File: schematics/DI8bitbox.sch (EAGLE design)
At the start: 20 parts, among them Q1 500mA/300V, X1 332-02, X2 332-02

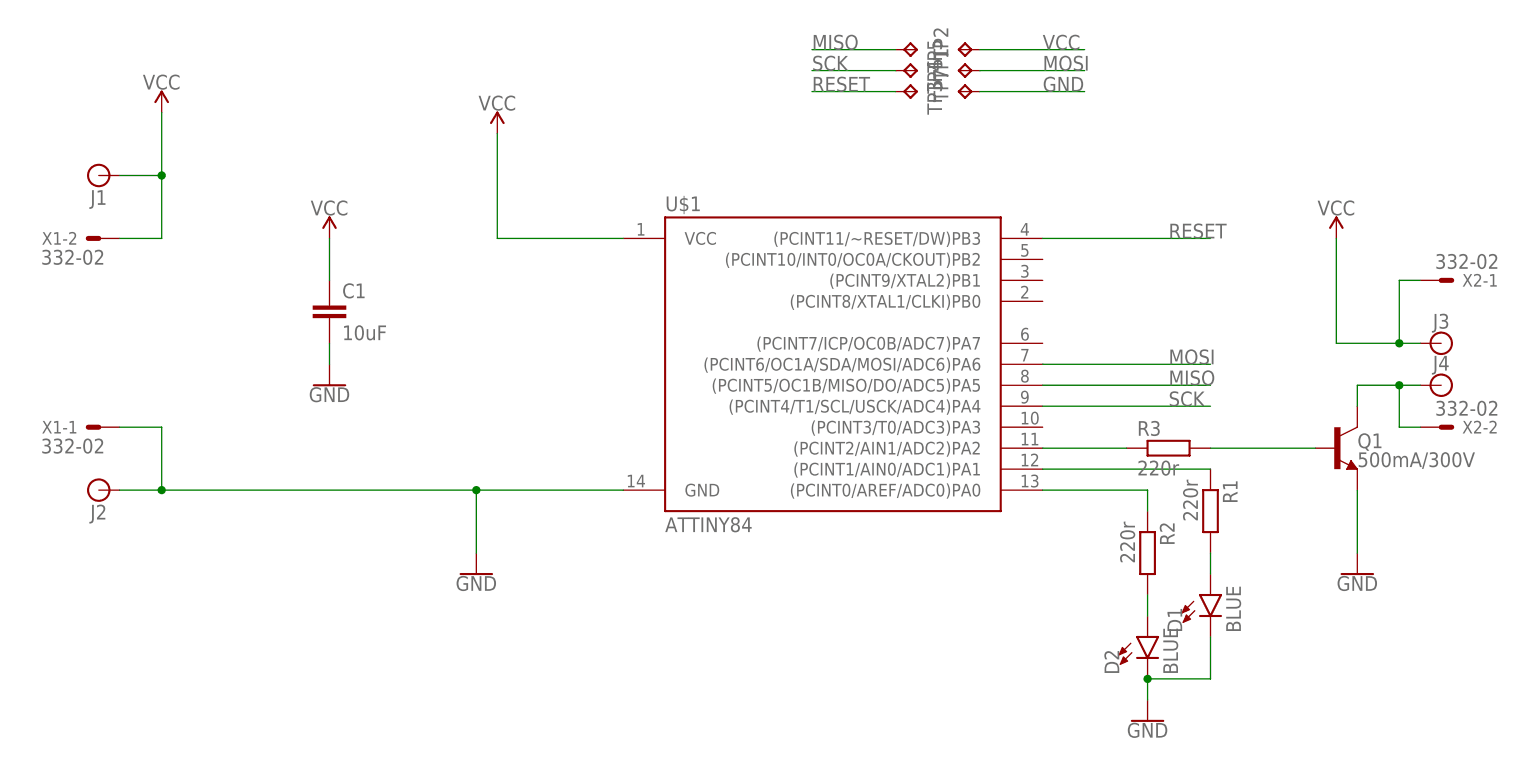
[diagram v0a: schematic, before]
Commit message: ordered rev.b at safepcb and mouser BOM updated
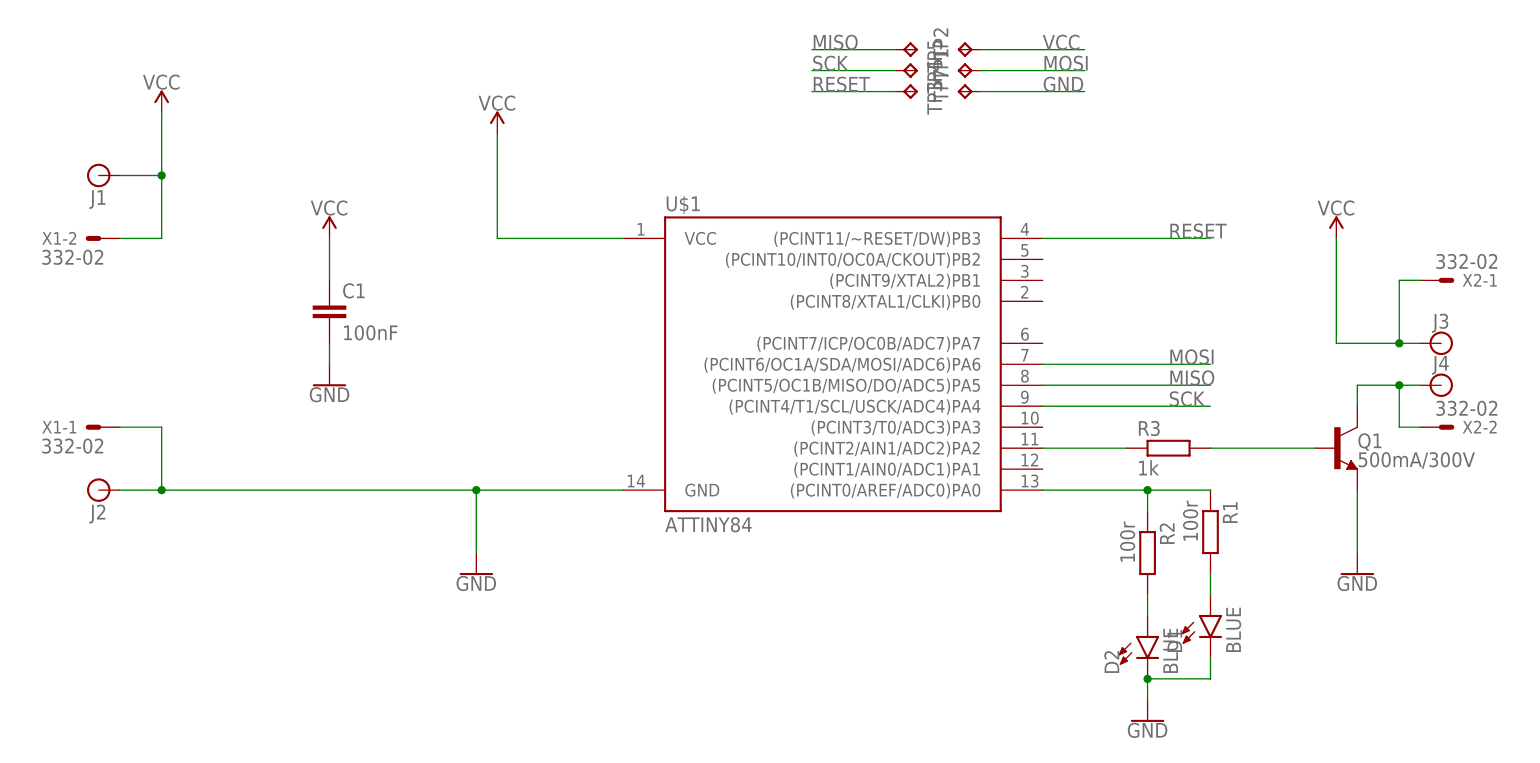
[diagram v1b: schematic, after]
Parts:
- C1: value 10uF -> 100nF; device SparkFun-Capacitors:10UF-1210-50V-20% -> SparkFun-Capacitors:10UF-1206-6.3V-20%
- R1, R2: value 220r -> 100r
- R3: value 220r -> 1k
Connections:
- removed net N$4: R1.1, U$1.(PCINT1/AIN0/ADC1)PA1
- net N$1: now also R1.1
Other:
- moved on the sheet: D1, R1
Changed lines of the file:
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@@
 <part name="GND1" library="SparkFun-PowerSymbols" deviceset="GND" device=""/>
 <part name="SUPPLY1" library="SparkFun-PowerSymbols" deviceset="VCC" device=""/>
-<part name="R1" library="rcl" deviceset="R-EU_" device="M0805" value="220r"/>
-<part name="R2" library="rcl" deviceset="R-EU_" device="M0805" value="220r"/>
+<part name="R1" library="rcl" deviceset="R-EU_" device="M0805" value="100r"/>
+<part name="R2" library="rcl" deviceset="R-EU_" device="M0805" value="100r"/>
 <part name="D1" library="SparkFun-LED" deviceset="LED-BLUE" device="1206" value="BLUE"/>
 <part name="D2" library="SparkFun-LED" deviceset="LED-BLUE" device="1206" value="BLUE"/>
@@
 <part name="SUPPLY4" library="SparkFun-PowerSymbols" deviceset="VCC" device=""/>
 <part name="GND5" library="SparkFun-PowerSymbols" deviceset="GND" device=""/>
-<part name="C1" library="SparkFun-Capacitors" deviceset="10UF" device="-1210-50V-20%" value="10uF"/>
+<part name="C1" library="SparkFun-Capacitors" deviceset="10UF" device="-1206-6.3V-20%" value="100nF"/>
 <part name="TP7" library="testpad" deviceset="TP" device="TP18R"/>
 <part name="TP1" library="testpad" deviceset="TP" device="TP18R"/>
@@
 <part name="J4" library="SparkFun-Connectors" deviceset="BANANA_CONN" device=""/>
 <part name="X2" library="con-garry" deviceset="332-02" device=""/>
-<part name="R3" library="rcl" deviceset="R-EU_" device="M0805" value="220r"/>
+<part name="R3" library="rcl" deviceset="R-EU_" device="M0805" value="1k"/>
 </parts>
 <sheets>
@@
 <instance part="GND1" gate="1" x="12.7" y="25.4"/>
 <instance part="SUPPLY1" gate="G$1" x="15.24" y="78.74"/>
-<instance part="R1" gate="G$1" x="101.6" y="33.02" rot="R270"/>
+<instance part="R1" gate="G$1" x="101.6" y="30.48" rot="R270"/>
 <instance part="R2" gate="G$1" x="93.98" y="27.94" rot="R270"/>
-<instance part="D1" gate="G$1" x="101.6" y="22.86"/>
+<instance part="D1" gate="G$1" x="101.6" y="20.32"/>
 <instance part="D2" gate="G$1" x="93.98" y="17.78"/>
 <instance part="GND3" gate="1" x="93.98" y="7.62"/>
@@
 <wire x1="93.98" y1="12.7" x2="93.98" y2="10.16" width="0.1524" layer="91"/>
 <pinref part="D1" gate="G$1" pin="C"/>
-<wire x1="101.6" y1="17.78" x2="101.6" y2="12.7" width="0.1524" layer="91"/>
+<wire x1="101.6" y1="15.24" x2="101.6" y2="12.7" width="0.1524" layer="91"/>
 <wire x1="101.6" y1="12.7" x2="93.98" y2="12.7" width="0.1524" layer="91"/>
 <junction x="93.98" y="12.7"/>
@@
 <pinref part="R2" gate="G$1" pin="1"/>
 <wire x1="93.98" y1="35.56" x2="93.98" y2="33.02" width="0.1524" layer="91"/>
+<pinref part="R1" gate="G$1" pin="1"/>
+<wire x1="93.98" y1="35.56" x2="101.6" y2="35.56" width="0.1524" layer="91"/>
+<junction x="93.98" y="35.56"/>
 </segment>
 </net>
@@
 <pinref part="R1" gate="G$1" pin="2"/>
 <pinref part="D1" gate="G$1" pin="A"/>
-<wire x1="101.6" y1="27.94" x2="101.6" y2="25.4" width="0.1524" layer="91"/>
-</segment>
-</net>
-<net name="N$4" class="0">
-<segment>
-<pinref part="R1" gate="G$1" pin="1"/>
-<pinref part="U$1" gate="G$1" pin="(PCINT1/AIN0/ADC1)PA1"/>
-<wire x1="101.6" y1="38.1" x2="81.28" y2="38.1" width="0.1524" layer="91"/>
-</segment>
-</net>
+<wire x1="101.6" y1="25.4" x2="101.6" y2="22.86" width="0.1524" layer="91"/>
+</segment>
+</net>
